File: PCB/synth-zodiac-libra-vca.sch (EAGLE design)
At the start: 29 parts, among them J4 6.35MM JACK, Q8 PNP, U2 LM13700

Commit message: Snapshot of designs so far.
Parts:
- removed C33: 2.2uF/16V, rlc:CAPACITOR_POL-ALUM-SMT-4
- removed J4: 6.35MM JACK, con-trs:TRS-JACK-STEREOTE-CK-6.35-29B
- removed JMP1, JMP2, JMP3, JMP4, JMP5, JMP6, JMP7: NP, rlc:RESISTOR0603
- removed JMP62: 0, rlc:RESISTOR0603
- removed R46, R48: 681R, rlc:RESISTOR0603
- removed R47: 33.2K, rlc:RESISTOR0603
- removed R49: 4.99K, rlc:RESISTOR0603
- removed R50, R54, R55: 10.0K, rlc:RESISTOR0603
- removed R51: 12.1K, rlc:RESISTOR0603
- removed R52: 475R, rlc:RESISTOR0603
- removed R53: 4.75M, rlc:RESISTOR0603
- removed R56: 499K, rlc:RESISTOR0603
- removed VCF_OUT: TPTHD-038, con-testpoints:TPTHD-038
- added +, -, A.OUT, A_BIAS, BUF.I, BUF.O, D_BIAS: PADSMD-050X050, con-testpoints:PADSMD-050X050
- added AUD_OUT_TS, TP_COW_IN, TP_VCF_IN: TPSMD-040-RND, con-testpoints:TPSMD-040-RND
- added A_OUT, COW_IN, EG_IN, VCF_IN: 2-pin, VT, SMT, con-jst:02PVT-SMT
- added C1: 2.2uF/16V, rlc:CAPACITOR_POL-ALUM-SMT-4
- added CONST: Libra, circuit-monkey-zodiac:CONSTELLATION-LIBRA
- added GLYPH: Libra, circuit-monkey-zodiac:GLYPH-LIBRA
- added J1: (no value), con-jst:04P-VT-SMT
- added JMP8: NP, rlc:SHORT0603
- added MODE: SPDT, switch-thd:SLIDE-SPDTSS-12-F45-TH-PCB
- added OUT: 6.35MM JACK, con-trs:TRS-JACK-STEREOPCB-PANEL
- added PCB: PCB FAB, circuit-monkey-zodiac:PENTAGON-40R
- added R1, R10, R2, R3, R4: 10.0K, rlc:RESISTOR0603
- added R11: 4.75M, rlc:RESISTOR0603
- added R12: 4.99K, rlc:RESISTOR0603
- added R13: 12.1K, rlc:RESISTOR0603
- added R14: 475R, rlc:RESISTOR0603
- added R5: 22.1K, rlc:RESISTOR0603
- added R6: 499K, rlc:RESISTOR0603
- added R7: 33.2K, rlc:RESISTOR0603
- added R8, R9: 681R, rlc:RESISTOR0603
- AUD_OUT, TP1: value TPTHD-038 -> TPSMD-040-RND; device con-testpoints:TPTHD-038 -> con-testpoints:TPSMD-040-RND
- GND_VCA: value TPTHD-SCOPE-LOOP -> TPSMD-040-RND; device con-testpoints:TPTHD-SCOPE-LOOP -> con-testpoints:TPSMD-040-RND
- renumbered C34 to C2, C35 to C3, U2 to U1
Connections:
- removed net N$71: JMP5.1, U1-A.OUT
- removed net N$72: JMP2.2, U1-A.DIODE-BIAS
- removed net N$74: JMP6.2, U1-A-BUFFER.IN
- removed net N$75: JMP7.1, U1-A-BUFFER.OUT
- new net AUDIO_OUT_TS: AUD_OUT_TS.P$1, A_OUT.1, OUT.TN
- new net COWBELL_IN: COW_IN.1, R2.1, TP_COW_IN.P$1
- new net EG_VCA: EG_IN.1, MODE-SW.A
- new net N$1: D_BIAS.PAD, U1-A.DIODE-BIAS
- new net N$142: MODE-SW.B, R5.1
- new net N$2: A.OUT.PAD, U1-A.OUT
- new net N$3: BUF.I.PAD, U1-A-BUFFER.IN
- new net N$4: BUF.O.PAD, U1-A-BUFFER.OUT
- new net VCF_IN: R1.1, TP_VCF_IN.P$1, VCF_IN.1
- net +9V: now also J1.1, R5.2, U1-PWR.V+; no longer U1-PWR.VDD
- net -9V: now also J1.2, R11.1, R13.1, R6.1, U1-PWR.V-; no longer R53.1, R56.1, U1-PWR.GND
- net AUDIO_OUT: now also OUT.T, R14.2; no longer J4.T, R52.2
- net EXP_VCA_CV: now also R4.1, R6.2; no longer R55.1, R56.2
- net GND: now also A_OUT.2, COW_IN.2, EG_IN.2, J1.4, MODE-MTG.MT1, MODE-MTG.MT2, OUT.S, PCB.GND@1, R12.1, R8.1, R9.1, VCF_IN.2; no longer J4.S, R46.1, R48.1, R49.1, R51.1
- net N$45: now also R9.2; no longer R46.2
- net N$60: now also R7.2, R8.2; no longer R47.2, R48.2
- net N$62: now also R12.2; no longer R49.2
- net N$63: now also R10.2; no longer R50.2
- net N$64: now also C1.P, R13.2; no longer C33.P, R51.2
- net N$65: now also C1.N, R14.1; no longer C33.N, R52.1
- net N$66: now also R10.1, R11.2; no longer R50.1, R53.2
- net N$67: now also JMP8.2; no longer JMP62.2
- net N$68: now also JMP8.1, R3.2, R4.2; no longer JMP62.1, R54.2, R55.2
- net N$69: now also -.PAD; no longer JMP1.2
- net N$70: now also +.PAD; no longer JMP3.2
- net N$73: now also A_BIAS.PAD; no longer JMP4.2
- net VCA_CV: now also MODE-SW.C, R3.1; no longer R54.1
- net VCF_OUT: now also R1.2, R2.2, R7.1; no longer R47.1, VCF_OUT.P$1
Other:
- note added: "===> AMP"
- note added: "Always on? Check orig schem."
- note added: "COW ===>"
- note added: "CV Panel ===>"
- note added: "EG ===>"
- note added: "NC"
- note added: "VCF ===>"
- moved on the sheet: AUD_OUT, GND_VCA, Q8, TP1

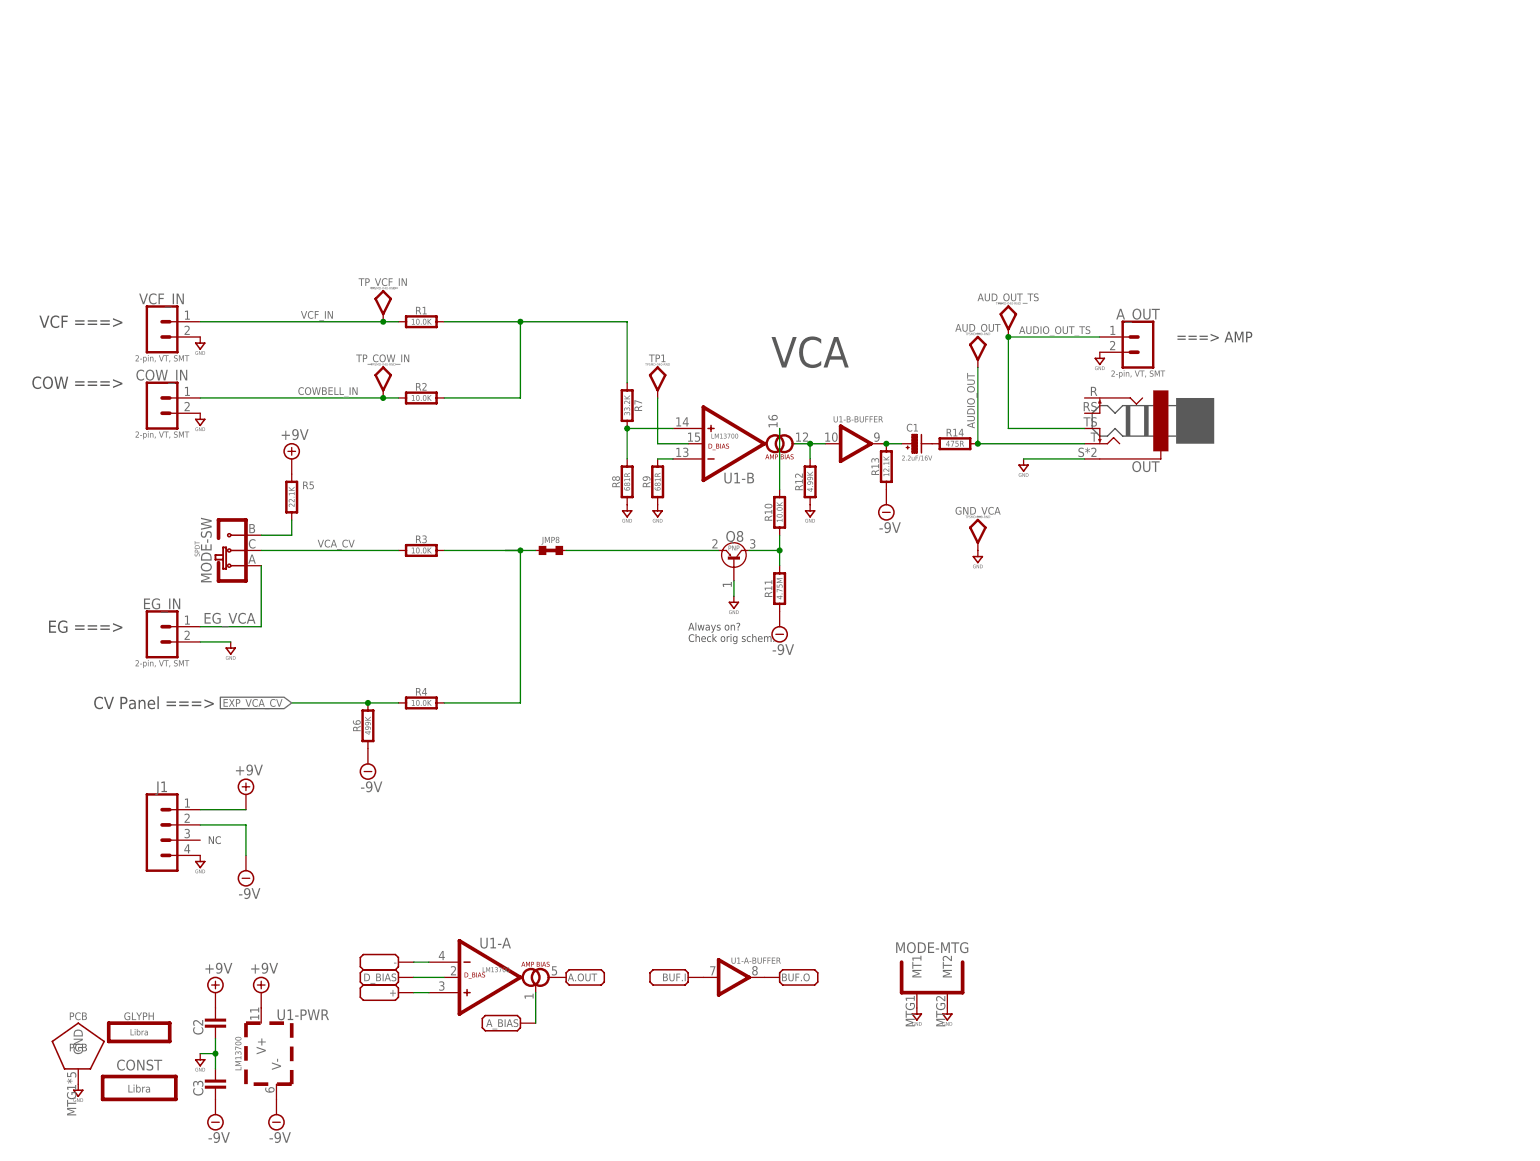
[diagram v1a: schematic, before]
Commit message: Almost ready for FAB.
Sagittarius was mis-spelled, renamed it.  Taurus is still WIP.
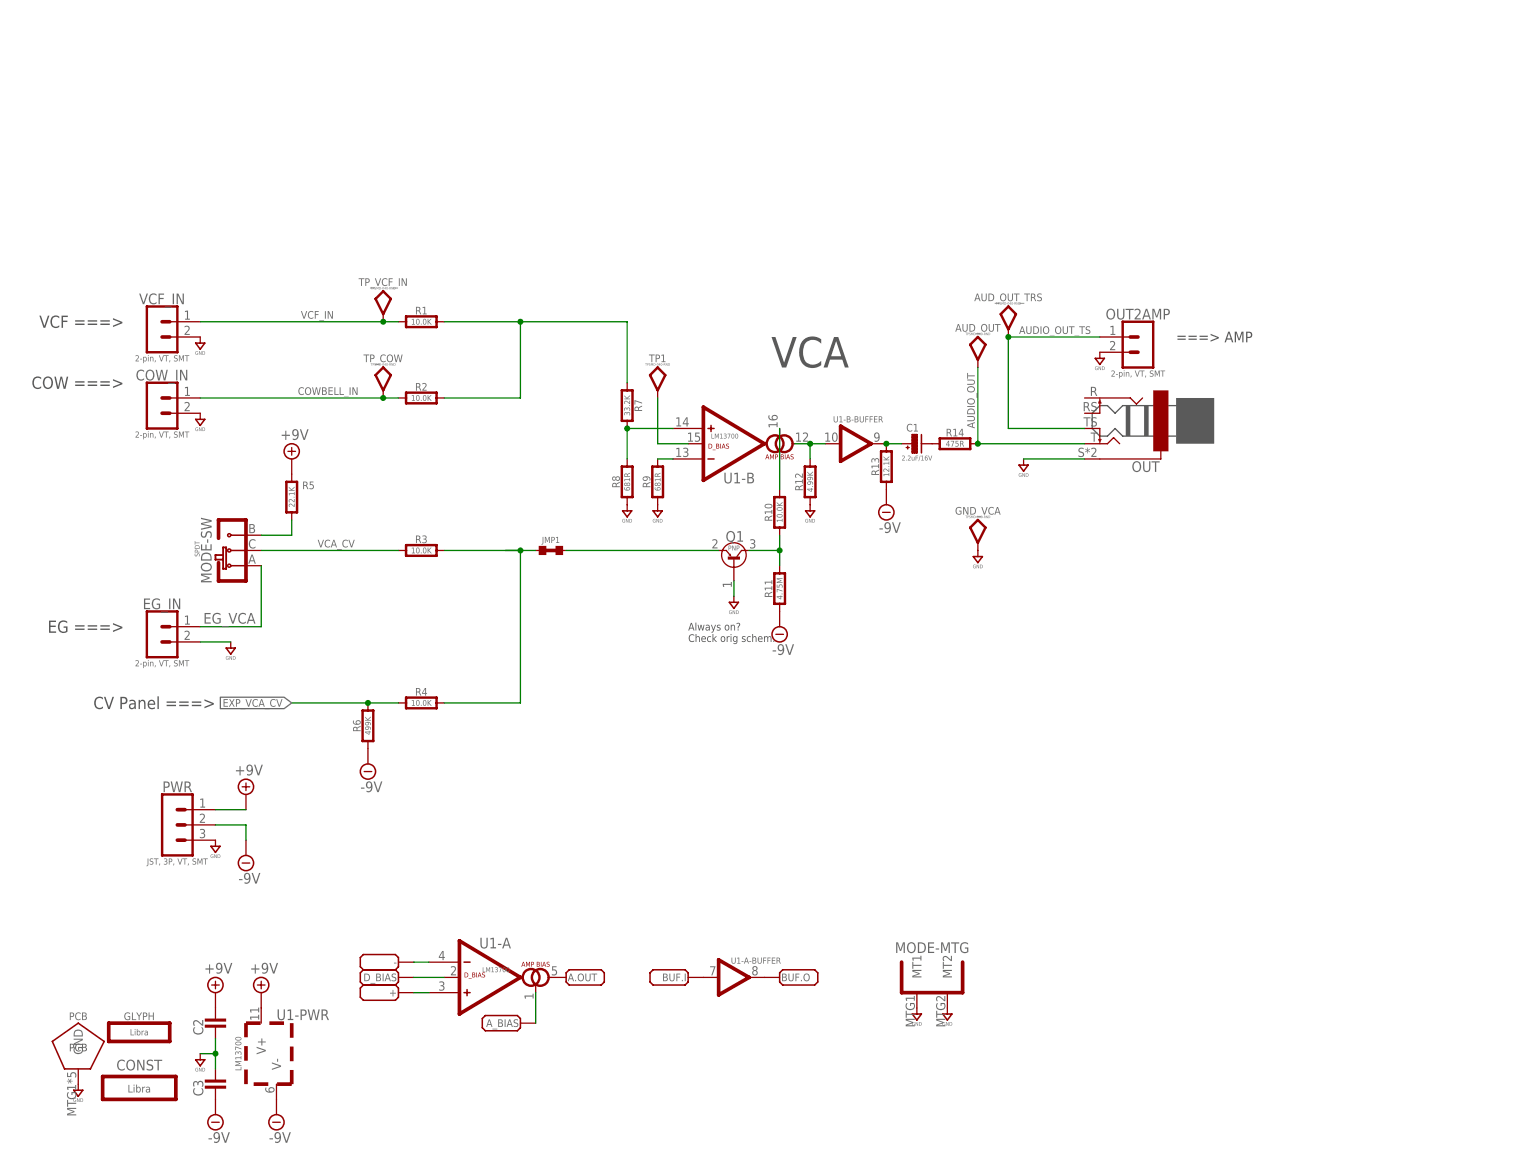
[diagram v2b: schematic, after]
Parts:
- removed J1: (no value), con-jst:04P-VT-SMT
- added PWR: JST, 3P, VT, SMT, con-jst:03P-VT-SMT
- renumbered AUD_OUT_TS to AUD_OUT_TRS, A_OUT to OUT2AMP, JMP8 to JMP1, Q8 to Q1, TP_COW_IN to TP_COW
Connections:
- net +9V: now also PWR.1; no longer J1.1
- net -9V: now also PWR.2; no longer J1.2
- net GND: now also PWR.3; no longer J1.4
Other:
- note removed: "NC"

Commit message: Work in progress for rev A,  VCO rev.B
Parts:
- removed +, -, A.OUT, A_BIAS, BUF.I, BUF.O, D_BIAS: PADSMD-050X050, con-testpoints:PADSMD-050X050
- removed JMP1: NP, rlc:SHORT0603
- removed R4: 10.0K, rlc:RESISTOR0603
- removed R6: 499K, rlc:RESISTOR0603
- COW_IN, EG_IN, OUT2AMP, VCF_IN: value 2-pin, VT, SMT -> JST, SH, 2P; device con-jst:02PVT-SMT -> con-jst:02P-SM-VT-SMT
- MODE: value SPDT -> (none); device switch-thd:SLIDE-SPDTSS-12-F45-TH-PCB -> switch-thd:SLIDE-SPDT-MNTSS-12-F45-TH-PCB
- PWR: value JST, 3P, VT, SMT -> JST SM 3P; device con-jst:03P-VT-SMT -> con-jst:03P-SM-VT-SMT
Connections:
- removed net EXP_VCA_CV: R4.1, R6.2
- removed net N$1: D_BIAS.PAD, U1-A.DIODE-BIAS
- removed net N$2: A.OUT.PAD, U1-A.OUT
- removed net N$3: BUF.I.PAD, U1-A-BUFFER.IN
- removed net N$4: BUF.O.PAD, U1-A-BUFFER.OUT
- removed net N$67: JMP1.2, Q1.EMITTER
- removed net N$69: -.PAD, U1-A.-
- removed net N$70: +.PAD, U1-A.+
- removed net N$73: A_BIAS.PAD, U1-A.AMP-BIAS
- net -9V: no longer R6.1
- net EG_VCA: now also MODE-SW.B; no longer MODE-SW.A
- net GND: now also U1-A-BUFFER.IN, U1-A.+, U1-A.-
- net N$142: now also MODE-SW.A; no longer MODE-SW.B
- net N$68: now also Q1.EMITTER; no longer JMP1.1, R4.2
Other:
- note added: "Libra"
- note added: "SATAN'S CYCLE WORKS"
- note added: "Zodiac Synth"
- note removed: "CV Panel ===>"
- moved on the sheet: MODE, PWR, R5

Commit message: Perhaps final Rev. A?
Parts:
- MODE: device switch-thd:SLIDE-SPDT-MNTSS-12-F45-TH-PCB -> switch-thd:SLIDE-SPDT-MNTSS-12-F45-TH-PCB-2
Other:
- moved on the sheet: MODE-MTG
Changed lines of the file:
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@@
 <part name="SUPPLY12" library="supply" library_urn="urn:adsk.eagle:library:10485988" deviceset="GND" device=""/>
 <part name="SUPPLY13" library="supply" library_urn="urn:adsk.eagle:library:10485988" deviceset="GND" device=""/>
-<part name="MODE" library="switch-thd" library_urn="urn:adsk.eagle:library:26242324" deviceset="SLIDE-SPDT-MNT" device="SS-12-F45-TH-PCB" package3d_urn="urn:adsk.eagle:package:36475164/3"/>
+<part name="MODE" library="switch-thd" library_urn="urn:adsk.eagle:library:26242324" deviceset="SLIDE-SPDT-MNT" device="SS-12-F45-TH-PCB-2"/>
 </parts>
 <sheets>
